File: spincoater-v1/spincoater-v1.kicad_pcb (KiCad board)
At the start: 2 copper layers, 135.5 x 149 mm, 37 parts, among them J1 KEYPAD_Conn_01x08_Pin, J2 POT_PIN28_Conn_01x03_Socket, J3 SDCARD_Conn_01x06_Socket, J4 POT_PIN27_Conn_01x03_Socket, J5 MOTOR_Conn_01x04_Pin, J6 LED1_Conn_01x02_Pin, J7 LED2_Conn_01x02_Pin, J8 12V_DC_Conn_01x02_Pin, J9 LCD_Conn_01x16_Socket, Q1 IRF9540N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

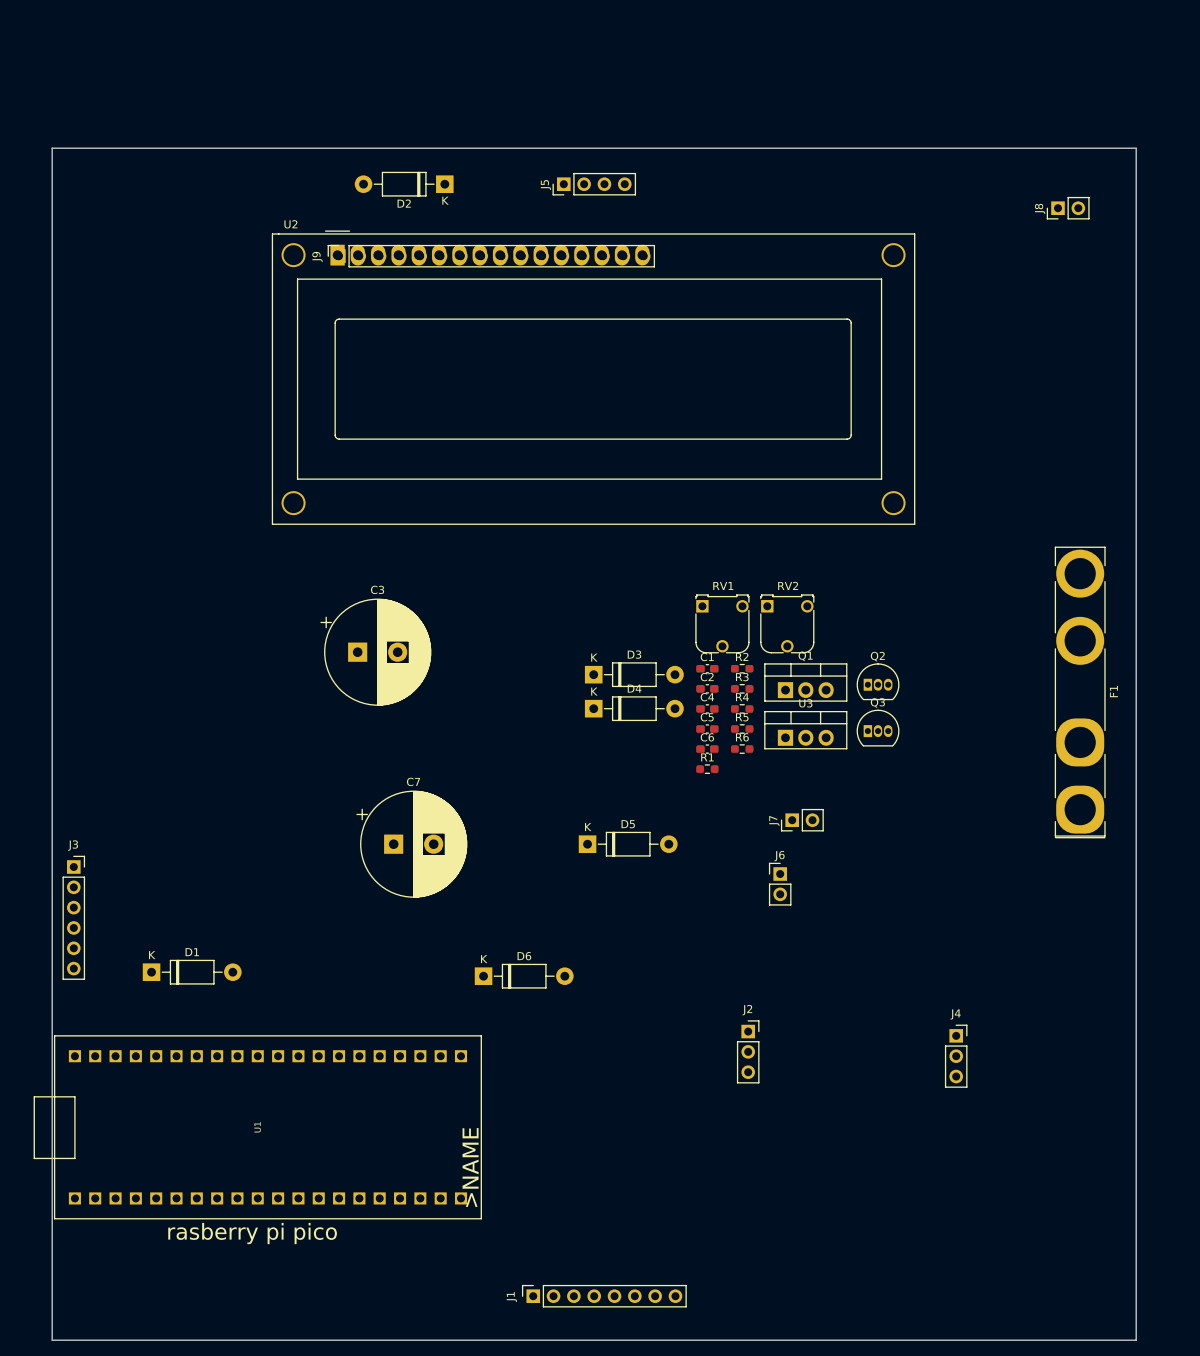
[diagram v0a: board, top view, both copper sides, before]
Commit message: Organized the pcb layout a bit, not sure if it is ideal. Ran the PCB through auto routing. Changed transistors to horizontal orrientation so that we can attach the LCD screen directly to the PCB. The capacitors might need to be changed, still don't know what size to use for it. Also might need to turn the capacitors horizontal for space saving purposes.
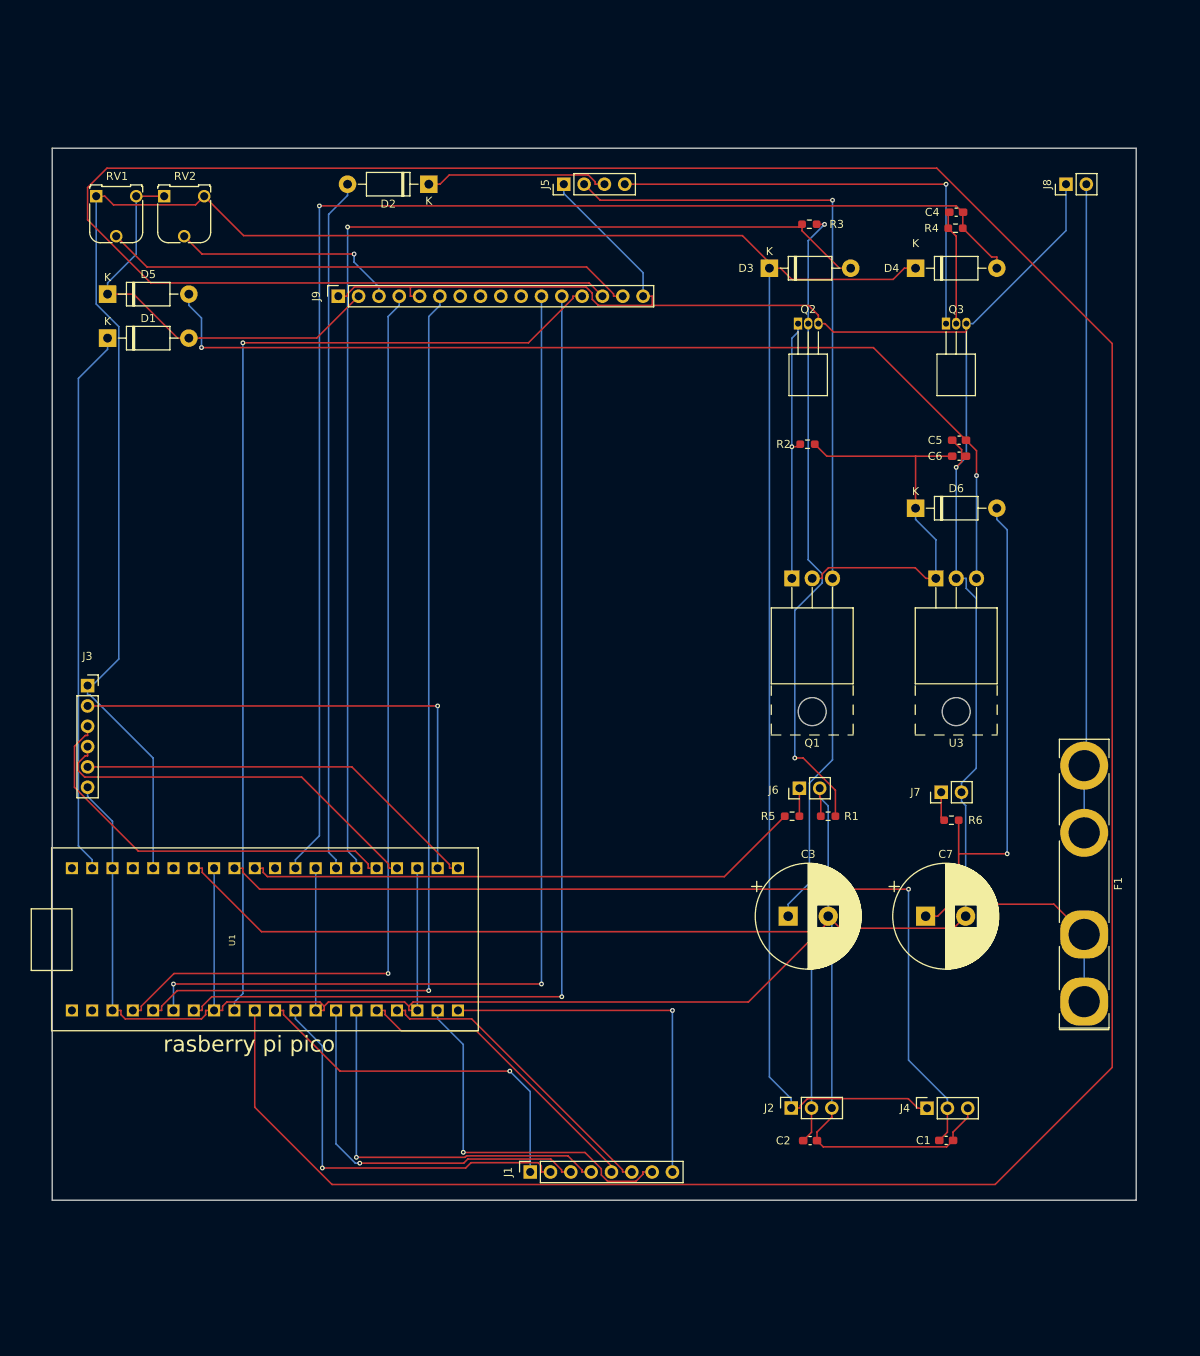
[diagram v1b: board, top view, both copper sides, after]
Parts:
- removed U2: LCD-16X2, Display:WC1602A
- J1: value KEYPAD_Conn_01x08_Pin -> KEYPAD
- J2: value POT_PIN28_Conn_01x03_Socket -> POT_PIN28
- J3: value SDCARD_Conn_01x06_Socket -> SDCARD
- J4: value POT_PIN27_Conn_01x03_Socket -> POT_PIN27
- J5: value MOTOR_Conn_01x04_Pin -> MOTOR
- J6: value LED1_Conn_01x02_Pin -> LED1
- J7: value LED2_Conn_01x02_Pin -> LED2
- J8: value 12V_DC_Conn_01x02_Pin -> 12V_DC
- J9: value LCD_Conn_01x16_Socket -> LCD
- Q1, U3: footprint Package_TO_SOT_THT:TO-220-3_Vertical -> Package_TO_SOT_THT:TO-220-3_Horizontal_TabUp
- Q2, Q3: footprint Package_TO_SOT_THT:TO-92_Inline -> Package_TO_SOT_THT:TO-92_Inline_Horizontal1
- moved RV1 91.5 mm to (66.0, 40.0)
- moved D5 91.3 mm to (67.4, 52.2)
- moved RV2 91.2 mm to (74.5, 40.0)
- moved D6 79.6 mm to (168.4, 79.0)
- moved D1 79.5 mm to (67.4, 57.7)
- moved C4 69.4 mm to (173.5, 42.0)
- moved D4 68.2 mm to (168.4, 49.0)
- moved C7 67.1 mm to (169.7, 130.0)
- moved C1 66.1 mm to (172.2, 158.0)
- moved R4 65.7 mm to (173.4, 44.0)
- moved C3 63.1 mm to (152.5, 130.0)
- moved R3 58.7 mm to (155.1, 43.5), turned to 180 degrees
- moved C2 57.9 mm to (155.2, 158.1)
- moved D3 55.4 mm to (150.2, 49.0)
- moved Q3 51.9 mm to (172.2, 55.9)
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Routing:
- net GND: track 0.00 -> 484.3 mm, vias 0 -> 1
- net /LCD.D7: track 0.00 -> 430.3 mm
- net +3.3V: track 0.00 -> 324.1 mm
- net /PWM_OUT: track 0.00 -> 174.0 mm, vias 0 -> 1
- net /MOTOR_EN: track 0.00 -> 146.4 mm, vias 0 -> 1
- net /LCD.D4: track 0.00 -> 135.3 mm, vias 0 -> 2
- net /LCD.D5: track 0.00 -> 134.6 mm, vias 0 -> 1
- net /LCD.D6: track 0.00 -> 128.9 mm, vias 0 -> 1
- net Net-(D5-A): track 0.00 -> 125.5 mm, vias 0 -> 2
- net /MOTOR_12V: track 0.00 -> 123.7 mm, vias 0 -> 1
- net /LCD.E: track 0.00 -> 123.2 mm, vias 0 -> 1
- net /GP27: track 0.00 -> 119.5 mm, vias 0 -> 1
- net /LCD.RS: track 0.00 -> 119.4 mm, vias 0 -> 1
- net /GP28: track 0.00 -> 107.4 mm, vias 0 -> 1
- net Net-(D6-A): track 0.00 -> 90.7 mm, vias 0 -> 1
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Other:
- board size 135.5 x 149 mm -> 135.5 x 131.5 mm

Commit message: added mounting holes for pcb, made it 2.6mm radius
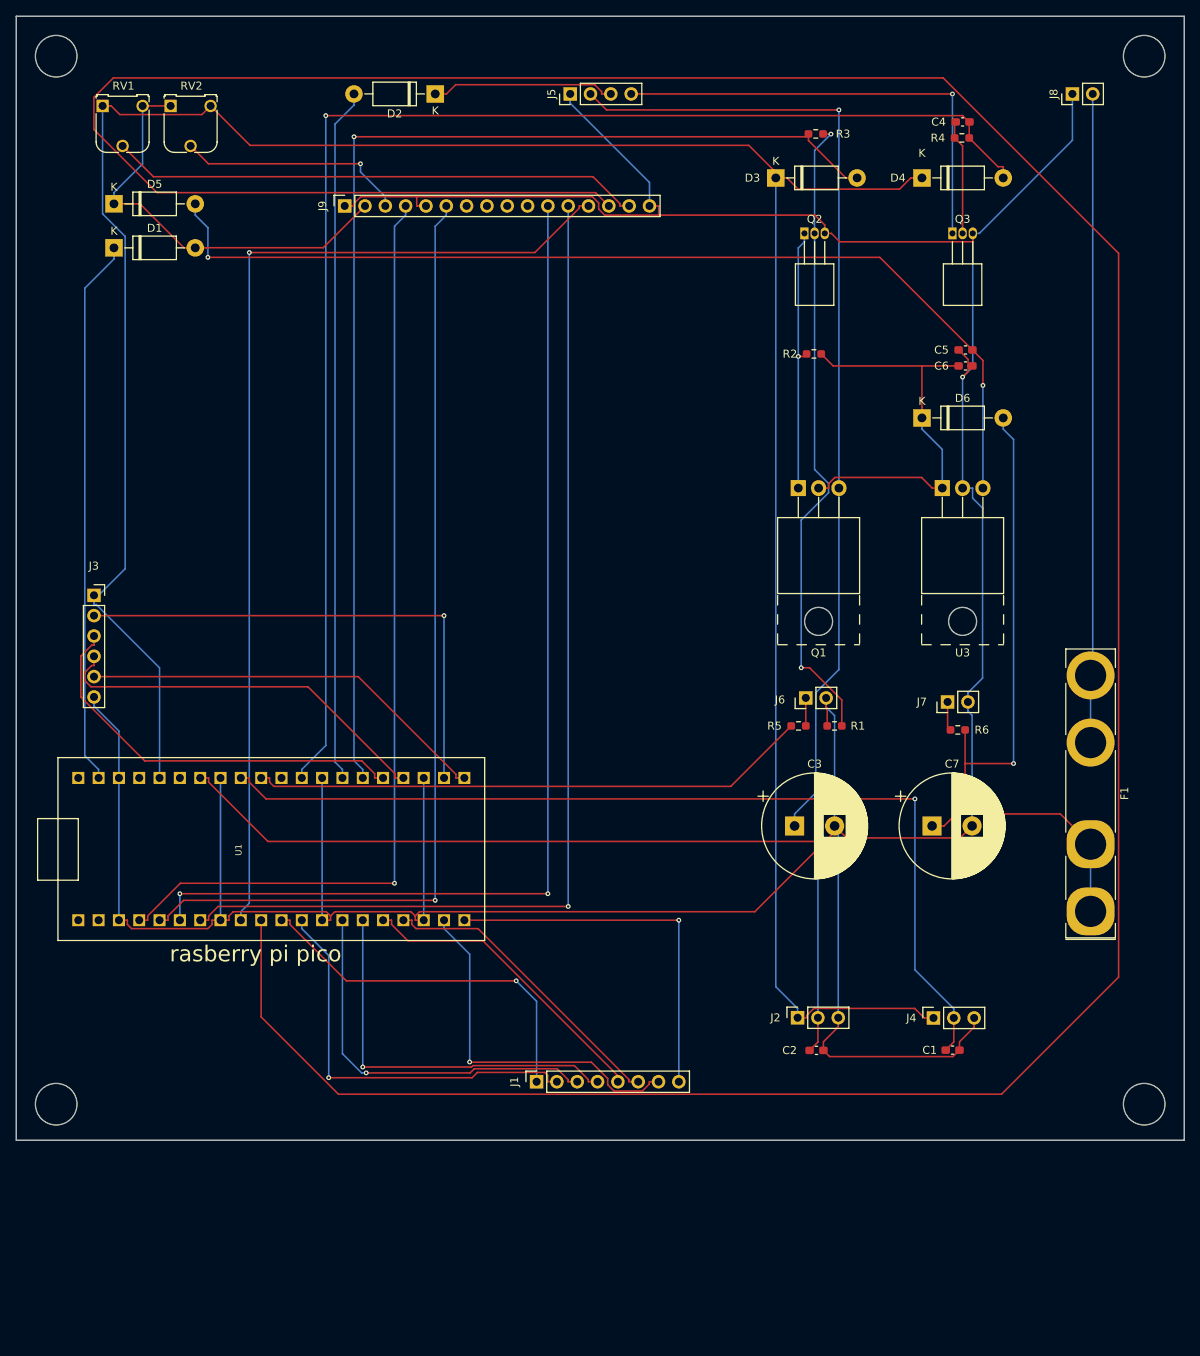
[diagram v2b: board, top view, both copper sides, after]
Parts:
- moved C1 11.3 mm to (173.0, 146.7)
- moved C2 11.3 mm to (156.0, 146.8)
- moved C3 11.3 mm to (153.3, 118.7)
- moved C7 11.3 mm to (170.5, 118.7)
- moved D6 11.3 mm to (169.2, 67.7)
- moved J7 11.3 mm to (172.4, 103.2)
- moved C4 11.3 mm to (174.3, 30.7)
- moved D1 11.3 mm to (68.2, 46.5)
- moved D5 11.3 mm to (68.2, 41.0)
- moved J6 11.3 mm to (154.7, 102.7)
- moved J8 11.3 mm to (188.0, 27.2)
- moved R1 11.3 mm to (158.3, 106.2)
- moved R5 11.3 mm to (153.8, 106.2)
- moved R6 11.3 mm to (173.7, 106.7)
- moved D2 11.3 mm to (108.4, 27.2)
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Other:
- board size 135.5 x 131.5 mm -> 146 x 140.5 mm
